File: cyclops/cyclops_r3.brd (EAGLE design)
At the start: 124.5 x 79.9 mm, 137 parts, among them Q1 BC817, Q2 IRF510, U1 MCP4921, U10 TLV2374, U11 THS4281, U12 MAX4564, U13 ZXTD, U14 ZXTD, U2 ADG3301, U3 MCP4022-50k, U4 LT1931, U5 LT1764A, U6 337L, U7 TLV3701, U8 ADR03, U9 OP1177, X1 SLP3, X2 SLP3, X3 SLP3

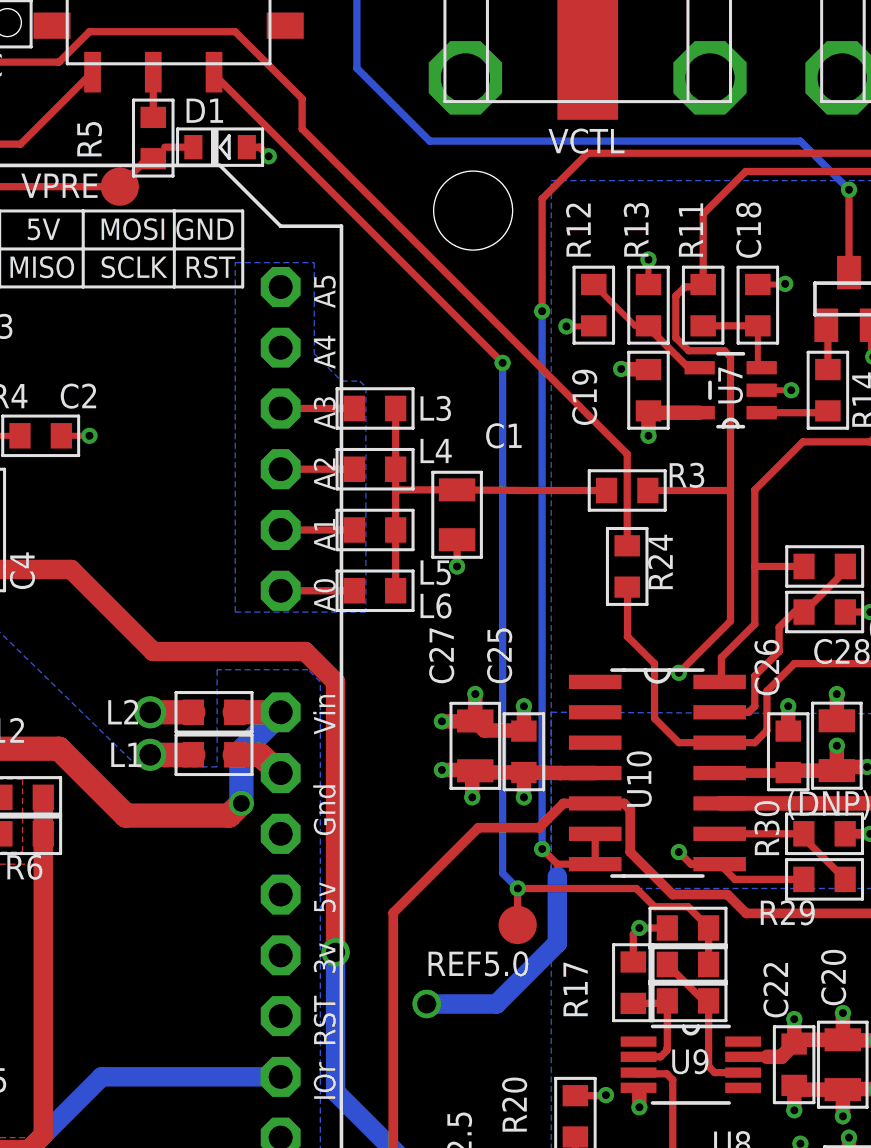
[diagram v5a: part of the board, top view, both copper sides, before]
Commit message: Fixed reference voltage issues.
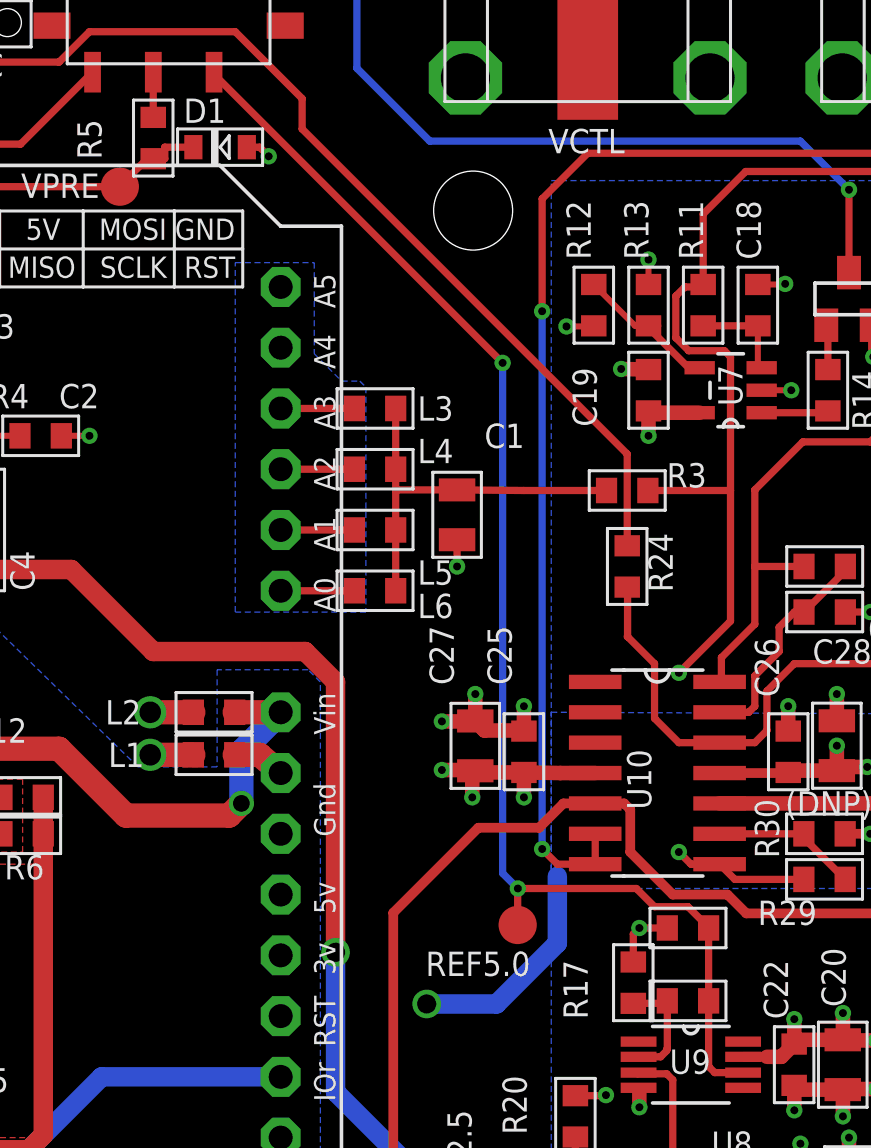
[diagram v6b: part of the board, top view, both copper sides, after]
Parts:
- removed R21: 1k, cyclops:0603
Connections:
- removed net VREFA2X1: R18.1, R21.1, U9.6
- net REF5.0: now also R18.1, U9.6; no longer R21.2
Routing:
- net VREFA2X1: track 6.65 -> 0.00 mm
- net REF5.0: track 51.1 -> 57.1 mm
- net VCTL: track 13.3 -> 14.5 mm
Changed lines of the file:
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@@
 <layer number="26" name="bNames" color="7" fill="1" visible="yes" active="yes"/>
 <layer number="27" name="tValues" color="7" fill="1" visible="yes" active="yes"/>
-<layer number="28" name="bValues" color="7" fill="1" visible="yes" active="yes"/>
+<layer number="28" name="bValues" color="7" fill="1" visible="no" active="yes"/>
 <layer number="29" name="tStop" color="7" fill="3" visible="no" active="yes"/>
 <layer number="30" name="bStop" color="7" fill="6" visible="no" active="yes"/>
@@
 <attribute name="VALUE" x="74.041" y="33.655" size="1.016" layer="27" font="vector" ratio="18" align="center-left"/>
 </element>
-<element name="R21" library="cyclops" package="0603" value="1k" x="72.517" y="35.179" smashed="yes">
-<attribute name="MN" value="Panasonic" x="73.914" y="37.973" size="0.8128" layer="27" font="vector" ratio="18" display="off"/>
-<attribute name="DK" value="PxxxxHTR-ND" x="73.914" y="37.973" size="0.8128" layer="27" font="vector" ratio="18" display="off"/>
-<attribute name="MPN" value="ERJ-3EKFxxxxV" x="73.914" y="37.973" size="0.8128" layer="27" font="vector" ratio="18" display="off"/>
-<attribute name="VALUE" x="74.041" y="35.179" size="1.016" layer="27" font="vector" ratio="18" align="center-left"/>
-</element>
 <element name="C24" library="cyclops" package="0603" value=".1uF" x="72.517" y="36.703" smashed="yes" rot="R180">
 <attribute name="VALUE" x="71.247" y="38.1" size="1.016" layer="27" font="vector" ratio="18" align="center-left"/>
@@
 <wire x1="43.18" y1="67.691" x2="41.91" y2="66.548" width="0.3048" layer="1"/>
 <wire x1="41.91" y1="66.548" x2="41.91" y2="63.373" width="0.3048" layer="1"/>
-<wire x1="50.165" y1="68.8594" x2="50.6476" y2="69.342" width="0" layer="19" extent="1-1"/>
-<wire x1="49.911" y1="68.8594" x2="50.165" y2="68.8594" width="0" layer="19" extent="1-1"/>
+<wire x1="50.165" y1="68.8594" x2="50.6476" y2="68.8594" width="0.3048" layer="1"/>
+<wire x1="50.6476" y1="68.8594" x2="50.6476" y2="69.342" width="0.3048" layer="1"/>
+<wire x1="50.165" y1="68.8594" x2="49.911" y2="68.8594" width="0.3048" layer="1"/>
 </signal>
 <signal name="N$6">
@@
 <signal name="REF5.0">
 <contactref element="TEST" pad="1"/>
-<contactref element="R21" pad="2"/>
-<contactref element="C24" pad="1"/>
-<contactref element="REF5.0" pad="TP"/>
-<wire x1="73.3806" y1="35.179" x2="73.3806" y2="36.703" width="0.3048" layer="1"/>
-<wire x1="73.3806" y1="36.703" x2="73.3806" y2="36.7284" width="0.3048" layer="1"/>
 <wire x1="73.3806" y1="36.7284" x2="72.517" y2="37.592" width="0.3048" layer="1"/>
 <wire x1="64.77" y1="60.325" x2="64.77" y2="38.989" width="0.3048" layer="16"/>
@@
 <wire x1="70.358" y1="38.354" x2="71.12" y2="37.592" width="0.3048" layer="1"/>
 <wire x1="71.12" y1="37.592" x2="72.517" y2="37.592" width="0.3048" layer="1"/>
-<wire x1="65.398" y1="36.83" x2="65.398" y2="38.347" width="0.3048" layer="1"/>
 <wire x1="65.398" y1="38.347" x2="65.405" y2="38.354" width="0.3048" layer="1"/>
 <via x="64.77" y="60.325" extent="1-16" drill="0.3302"/>
 <wire x1="64.77" y1="60.325" x2="52.707" y2="72.388" width="0.3048" layer="1"/>
 <wire x1="52.707" y1="72.388" x2="52.707" y2="72.477" width="0.3048" layer="1"/>
+<contactref element="R18" pad="1"/>
+<contactref element="U9" pad="6"/>
+<contactref element="C24" pad="1"/>
+<contactref element="REF5.0" pad="TP"/>
+<wire x1="74.8214" y1="30.6578" x2="73.6346" y2="30.6578" width="0.3048" layer="1"/>
+<wire x1="73.6346" y1="30.6578" x2="73.3806" y2="30.9118" width="0.3048" layer="1"/>
+<wire x1="73.3806" y1="30.9118" x2="73.3806" y2="33.655" width="0.3048" layer="1"/>
+<wire x1="73.3806" y1="33.655" x2="73.1774" y2="33.655" width="0.3048" layer="1"/>
+<wire x1="73.3806" y1="33.655" x2="73.3806" y2="36.703" width="0.3048" layer="1"/>
+<wire x1="73.3806" y1="36.703" x2="73.3806" y2="36.7284" width="0.3048" layer="1"/>
+<wire x1="65.405" y1="38.354" x2="65.398" y2="38.354" width="0.3048" layer="1"/>
+<wire x1="65.398" y1="38.354" x2="65.398" y2="36.83" width="0.3048" layer="1"/>
 </signal>
 <signal name="N$3">
@@
 <signal name="N$17">
 </signal>
-<signal name="VREFA2X1">
-<contactref element="R18" pad="1"/>
-<contactref element="R21" pad="1"/>
-<contactref element="U9" pad="6"/>
-<wire x1="74.8214" y1="30.6578" x2="73.6346" y2="30.6578" width="0.3048" layer="1"/>
-<wire x1="73.6346" y1="30.6578" x2="73.3806" y2="30.9118" width="0.3048" layer="1"/>
-<wire x1="73.3806" y1="30.9118" x2="73.3806" y2="33.655" width="0.3048" layer="1"/>
-<wire x1="73.3806" y1="33.655" x2="73.1774" y2="33.655" width="0.3048" layer="1"/>
-<wire x1="73.1774" y1="33.655" x2="71.6534" y2="35.179" width="0.3048" layer="1"/>
-</signal>
 <signal name="N$18">
